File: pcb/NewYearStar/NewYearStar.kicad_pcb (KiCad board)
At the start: 2 copper layers, 28.7 x 51.4 mm, 22 parts, among them J1 Conn_01x03_Male, J2 Conn_01x02_Male, J3 Conn_01x02_Male, J4 Conn_01x02_Male, J5 Conn_01x02_Male

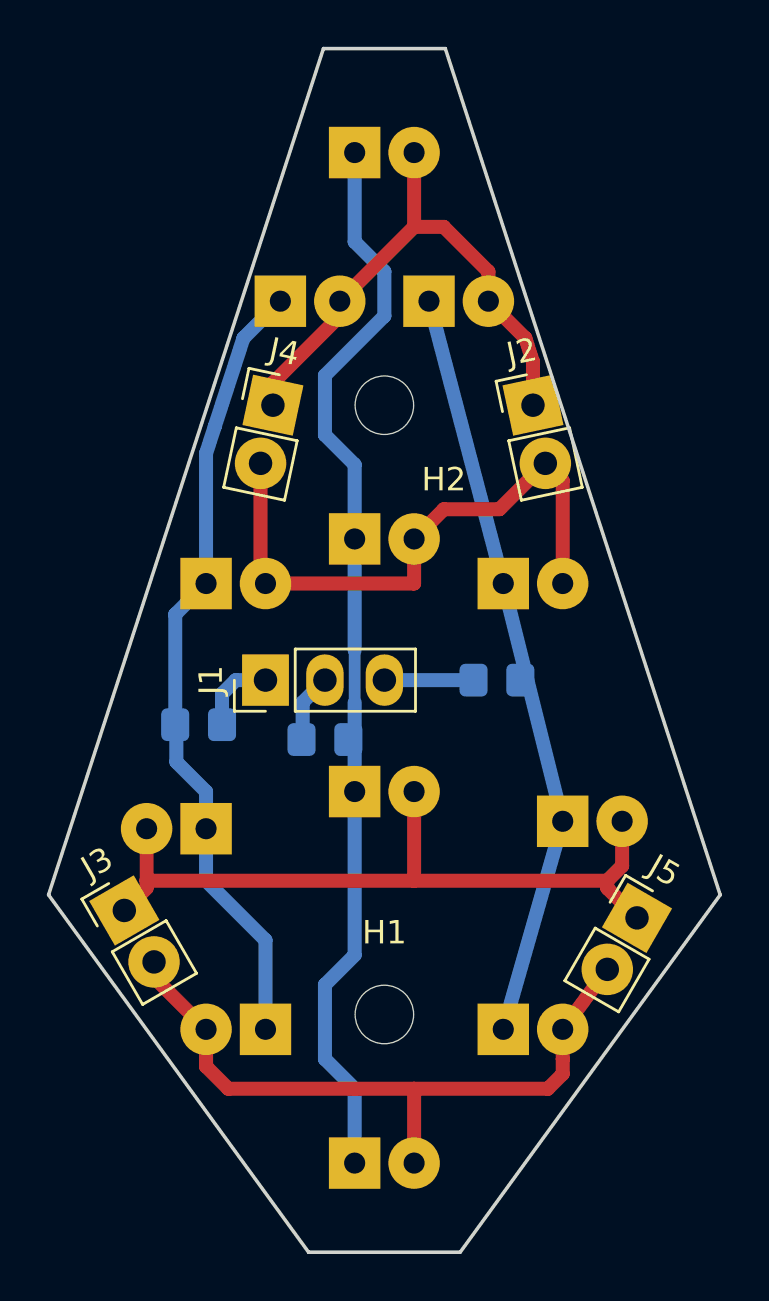
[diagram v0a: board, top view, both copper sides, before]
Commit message: Add R for every LED
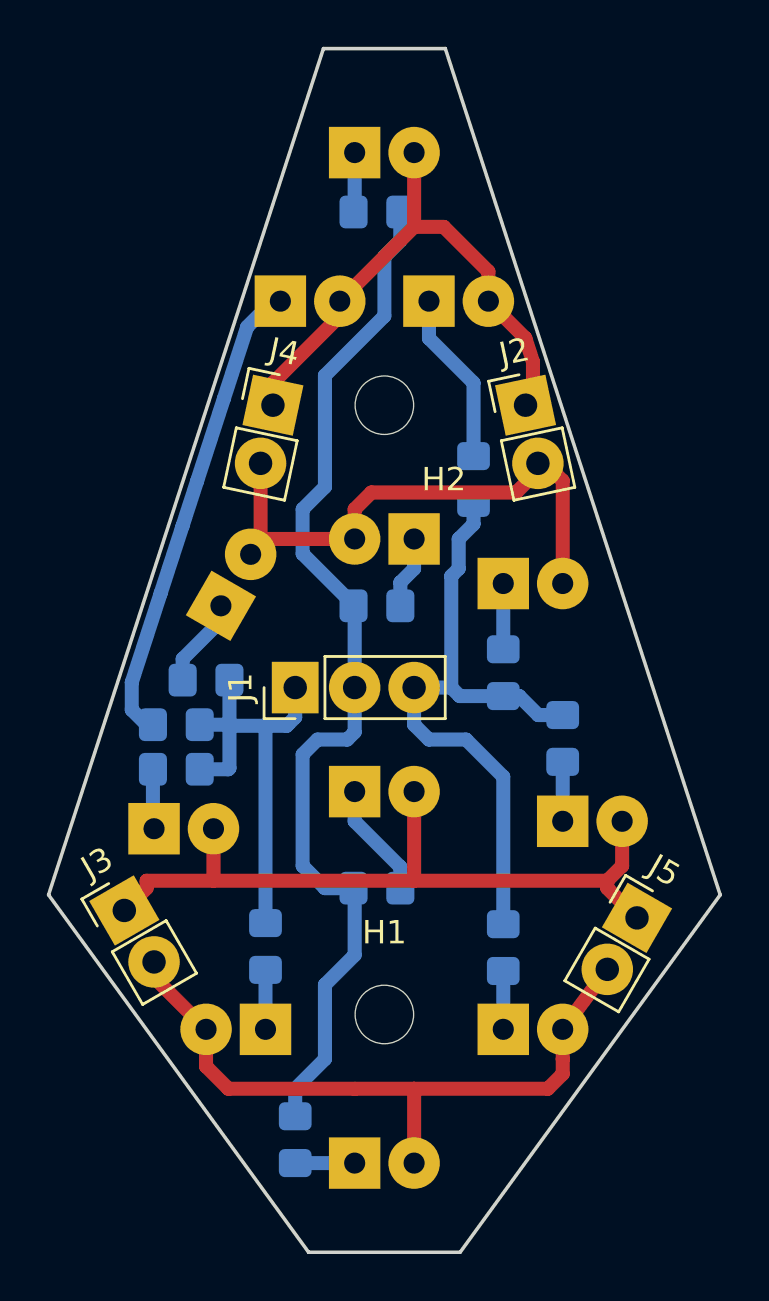
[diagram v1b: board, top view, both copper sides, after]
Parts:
- added R10: 130, Resistor_SMD:R_0805_2012Metric_Pad1.20x1.40mm_HandSolder, B.Cu at (106.7, 72.4)
- added R11: 130, Resistor_SMD:R_0805_2012Metric_Pad1.20x1.40mm_HandSolder, B.Cu at (109.2, 75.2)
- added R12: 130, Resistor_SMD:R_0805_2012Metric_Pad1.20x1.40mm_HandSolder, B.Cu at (106.7, 84.1)
- added R4: 130, Resistor_SMD:R_0805_2012Metric_Pad1.20x1.40mm_HandSolder, B.Cu at (96.5, 84.1)
- added R5: 130, Resistor_SMD:R_0805_2012Metric_Pad1.20x1.40mm_HandSolder, B.Cu at (101.3, 52.7)
- added R6: 130, Resistor_SMD:R_0805_2012Metric_Pad1.20x1.40mm_HandSolder, B.Cu at (101.3, 69.5)
- added R7: 130, Resistor_SMD:R_0805_2012Metric_Pad1.20x1.40mm_HandSolder, B.Cu at (101.3, 81.6)
- added R8: 130, Resistor_SMD:R_0805_2012Metric_Pad1.20x1.40mm_HandSolder, B.Cu at (97.8, 92.3)
- added R9: 130, Resistor_SMD:R_0805_2012Metric_Pad1.20x1.40mm_HandSolder, B.Cu at (105.4, 64.1)
- R1, R2, R3: value 510 -> 130
- moved R3 14.2 mm to (92.7, 76.5), turned to 0 degrees
- moved R2 5.68 mm to (94.0, 72.7), turned to 0 degrees
- moved D6 2.54 mm to (102.9, 66.7), turned to 180 degrees
- moved D3 2.22 mm to (91.8, 79.1), turned to 0 degrees
- moved J1 1.31 mm to (97.8, 73.0)
- moved D2 1.14 mm to (94.6, 69.5), turned to 60 degrees
- moved R1 0.95 mm to (92.7, 74.6)
- moved J2 0.32 mm to (107.6, 61.0)
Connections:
- D11 pad 1: Net-(D10-Pad1) -> Net-(D11-Pad1)
- D12 pad 1: Net-(D10-Pad1) -> Net-(D12-Pad1)
- D2 pad 1: Net-(D1-Pad1) -> Net-(D2-Pad1)
- D3 pad 1: Net-(D1-Pad1) -> Net-(D3-Pad1)
- D4 pad 1: Net-(D1-Pad1) -> Net-(D4-Pad1)
- D6 pad 1: Net-(D5-Pad1) -> Net-(D6-Pad1)
- D7 pad 1: Net-(D5-Pad1) -> Net-(D7-Pad1)
- D8 pad 1: Net-(D5-Pad1) -> Net-(D8-Pad1)
- D9 pad 1: Net-(D10-Pad1) -> Net-(D9-Pad1)
- R2 pad 1: Net-(D5-Pad1) -> Net-(D2-Pad1)
- R2 pad 2: Net-(J1-Pad2) -> Net-(J1-Pad1)
- R3 pad 1: Net-(D10-Pad1) -> Net-(D3-Pad1)
- R3 pad 2: Net-(J1-Pad3) -> Net-(J1-Pad1)
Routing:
- net Net-(D5-Pad1): track 46.3 -> 2.56 mm
- net Net-(J1-Pad2): track 2.95 -> 45.6 mm
- net Net-(D10-Pad1): track 33.3 -> 2.81 mm
- net Net-(J1-Pad3): track 3.81 -> 27.7 mm
- net Net-(J1-Pad1): track 3.42 -> 19.0 mm
- net Net-(D1-Pad1): track 34.8 -> 20.2 mm
- net Net-(D9-Pad1): track 0.00 -> 8.49 mm
- net Net-(D7-Pad1): track 0.00 -> 4.94 mm
- net Net-(D2-Pad1): track 0.00 -> 3.85 mm
- net Net-(D6-Pad1): track 0.00 -> 3.10 mm
- net Net-(D3-Pad1): track 0.00 -> 2.56 mm
- net Net-(D8-Pad1): track 0.00 -> 2.54 mm
- net Net-(D4-Pad1): track 0.00 -> 2.54 mm
- net Net-(D11-Pad1): track 0.00 -> 2.54 mm
- net Net-(D12-Pad1): track 0.00 -> 2.49 mm
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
